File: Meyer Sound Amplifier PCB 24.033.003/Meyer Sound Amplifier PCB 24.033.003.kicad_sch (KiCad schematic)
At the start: 80 parts, among them Q10 KSP92, Q11 KSP92, Q1A IRFP940, Q2A IRFP9240, Q3A TIP29CG, Q4A IRFP914, Q5A IRFP9140, Q6A FEP16BT, Q7A FEP16BT, Q8A TIP50G, Q9 MPSA42, U1 NE5532, U2 LF347N, U3 LM339

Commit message: fix some small errors and missing values
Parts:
- added C18, C23, C24: 1u, symbol Device:C_Small
- added C21, C22: 100n, symbol Device:C_Small
- C1, C5, C6: value ~ -> 470p
- C12: renamed from C12?; value ~ -> 470p
- C13: value 1n -> 1n6
- C14: renamed from C14?; value ~ -> 100n
- C19: renamed from C13??; value ~ -> 100n
- C20: value ~ -> 100n
- C4, C9: value C_Foil -> 22n 250V
- D1, D11, D7: value 10V -> 10V 1N5240B
- D12, D6, D9: value ~ -> 1N4936
- D13: value ~ -> 8.2V? 1N5237B?
- D4: value D_Zener_Dual_CommonCathode_AKA -> 10V 1N5240B
- D5: value ~ -> 10V 1N5240B
- D8: value 10V -> 16V 1N4745
- Q1A: value IRFP940 -> IRFP240
- Q4A: value IRFP914 -> IRFP140
- R23: value 1k/110? -> 1k
- R26: value 3k32? -> 3k32
- VR1: value ~ -> 10k
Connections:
- net GNDA: now also C12.1; no longer R17.1, R18AB.2, R18B.1
- net GNDB: now also R18AB.2, R18B.1
- net at R17.2: now also D11.2 (A), Q5A.1 (G), R16.1; no longer C12.1
- new net: C12.2, R17.1
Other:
- moved on the sheet: C1, C12, C4, D10, D11, D2, D9, Q8A, R1, R16, R17, R2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

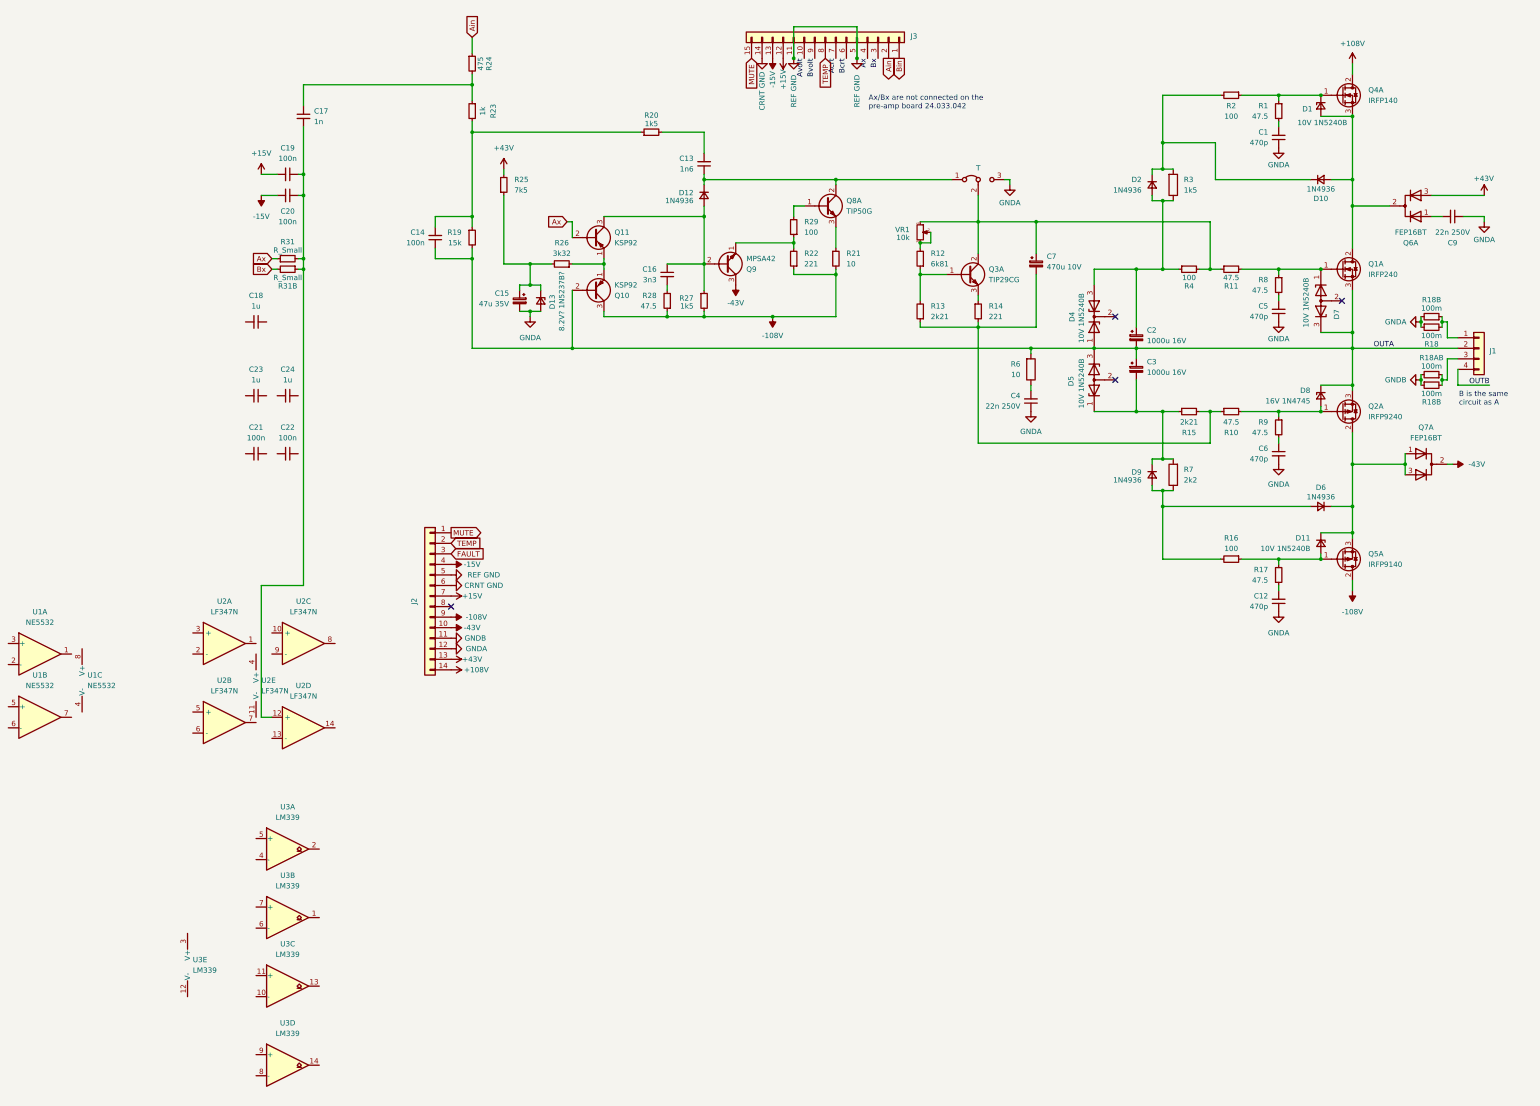
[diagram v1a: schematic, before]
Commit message: some more rev eng and better grouping of parts
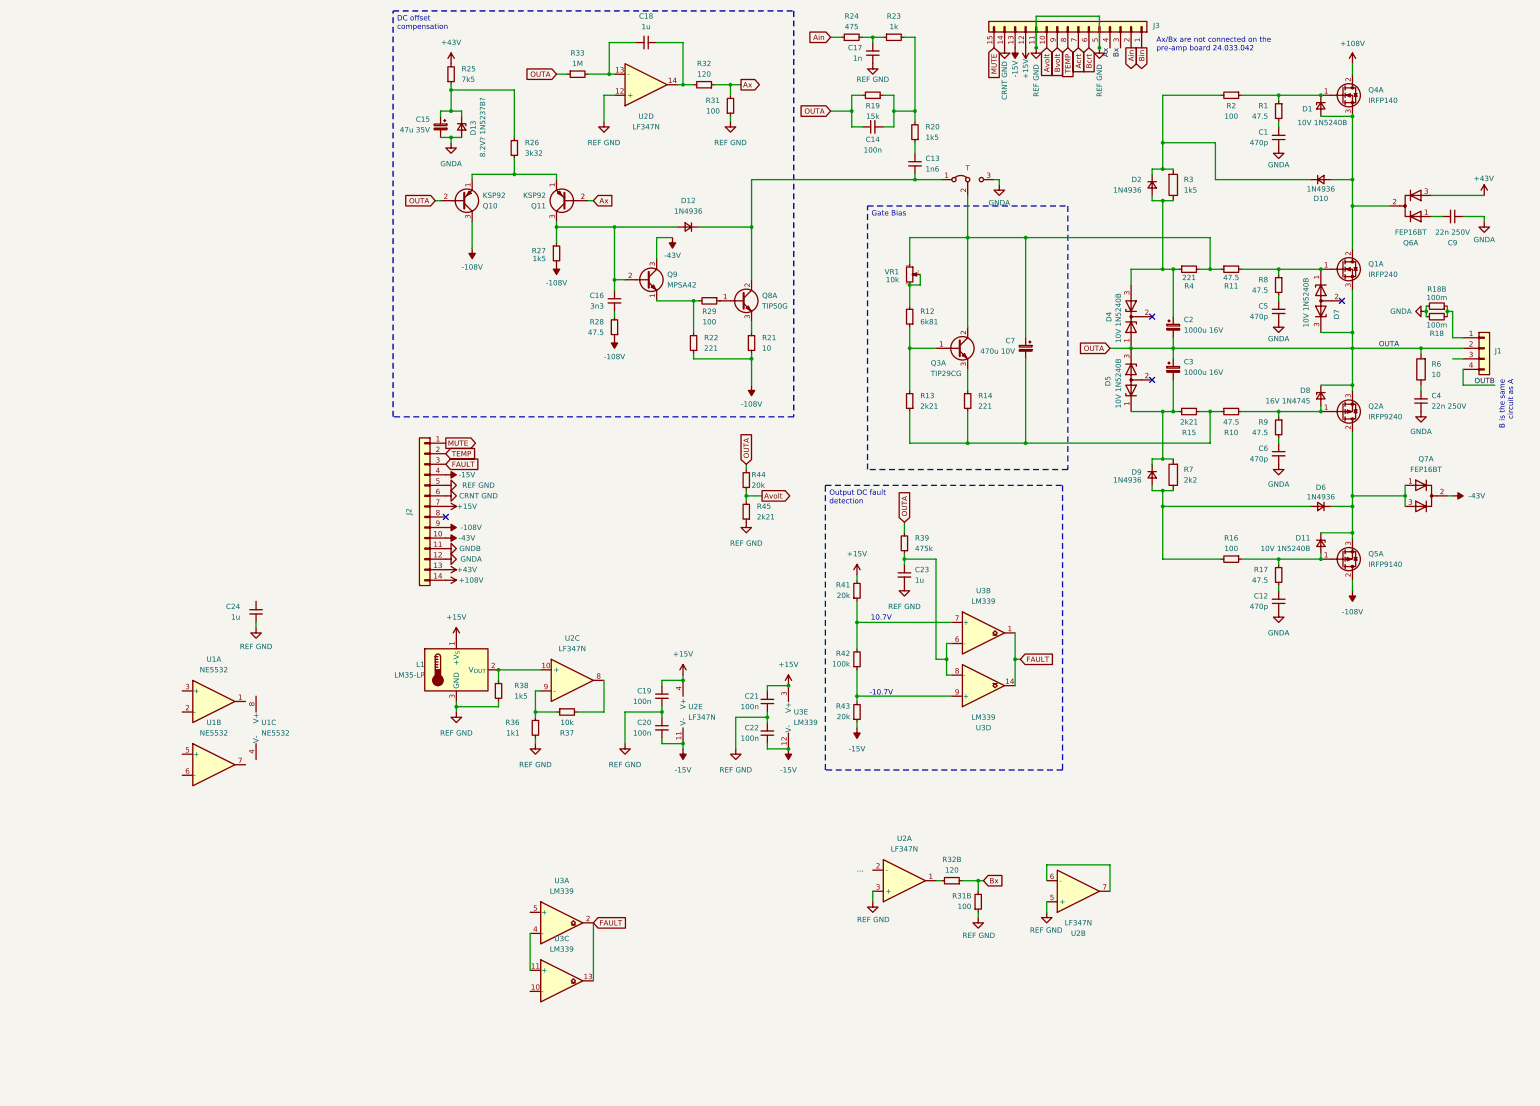
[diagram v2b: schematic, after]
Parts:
- removed R18AB, R18B: 100m, symbol Device:R_Small
- added L1: LM35-LP, Package_TO_SOT_THT:TO-92_Inline, symbol Sensor_Temperature:LM35-LP
- added R32, R32B: 120, symbol Device:R_Small
- added R33: 1M, symbol Device:R_Small
- added R36: 1k1, symbol Device:R_Small
- added R37: 10k, symbol Device:R_Small
- added R38: 1k5, symbol Device:R_Small
- added R39: 475k, symbol Device:R_Small
- added R41, R43, R44: 20k, symbol Device:R_Small
- added R42: 100k, symbol Device:R_Small
- added R45: 2k21, symbol Device:R_Small
- R31, R31B: value R_Small -> 100
- R4: value 100 -> 221
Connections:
- net +15V: now also C19.1, C21.2, U2.4 (V+), U3.3 (V+), L1.1 (+V_{S}), R41.2; no longer C19.2
- net -15V: now also C22.1, U2.11 (V-), U3.12 (V-), R43.1
- net Avolt: now also R44.1, R45.2
- net Ax: now also R31.2, R32.1; no longer R31.1
- net Bx: now also R32B.1
- net FAULT: now also U3.1, U3.13, U3.14, U3.2
- net OUTA: now also R33.1, R39.2, R44.2
- net REF GND: now also C17.1, C19.2, C20.1, C21.1, C22.2, C23.2, C24.2, R31.1, R31B.1, U2.12 (+), U2.3 (+), U2.5 (+), L1.3 (GND), R36.2, R38.2, R45.1
- net at U3.8 (-): now also C23.1, U3.6 (-), R39.1
- net at U3.9 (+): now also R42.1, R43.2
- net at D12.1 (K), Q8A.2 (C), T.1 (A): now also C13.2; no longer C13.1
- net at R20.2: now also C14.2, R19.1, R23.2; no longer C13.2
- net at Q9.1 (E), R22.2: now also R29.2; no longer R29.1
- net at Q8A.1 (B): now also R29.1; no longer R29.2
- net at U3.4 (-): now also U3.11 (+)
- net at C15.1, D13.1 (K), R25.1: now also R26.1; no longer R26.2
- net at C18.1: now also U2.14, R32.2
- net at C18.2: now also U2.13 (-), R33.2
- net at R23.1, R24.2: now also C17.2; no longer C17.1
- net at U3.7 (+): now also R41.1, R42.2
- net at U2.10 (+): now also L1.2 (V_{OUT}), R38.1
- net at U2.8: now also R37.2
- net at U2.9 (-): now also R36.1, R37.1
- net at Q10.1 (E), Q11.1 (E): now also R26.2; no longer R26.1
- net at U2.6 (-): now also U2.7
- net at U2.1: now also R32B.2
- new net: C13.1, R20.1
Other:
- note added: "-10.7V"
- note added: "..."
- note added: "10.7V"
- moved on the sheet: C13, C14, C15, C16, C17, C18, C19, C2, C20, C21, C22, C23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

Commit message: add current feedback and some minor fixes
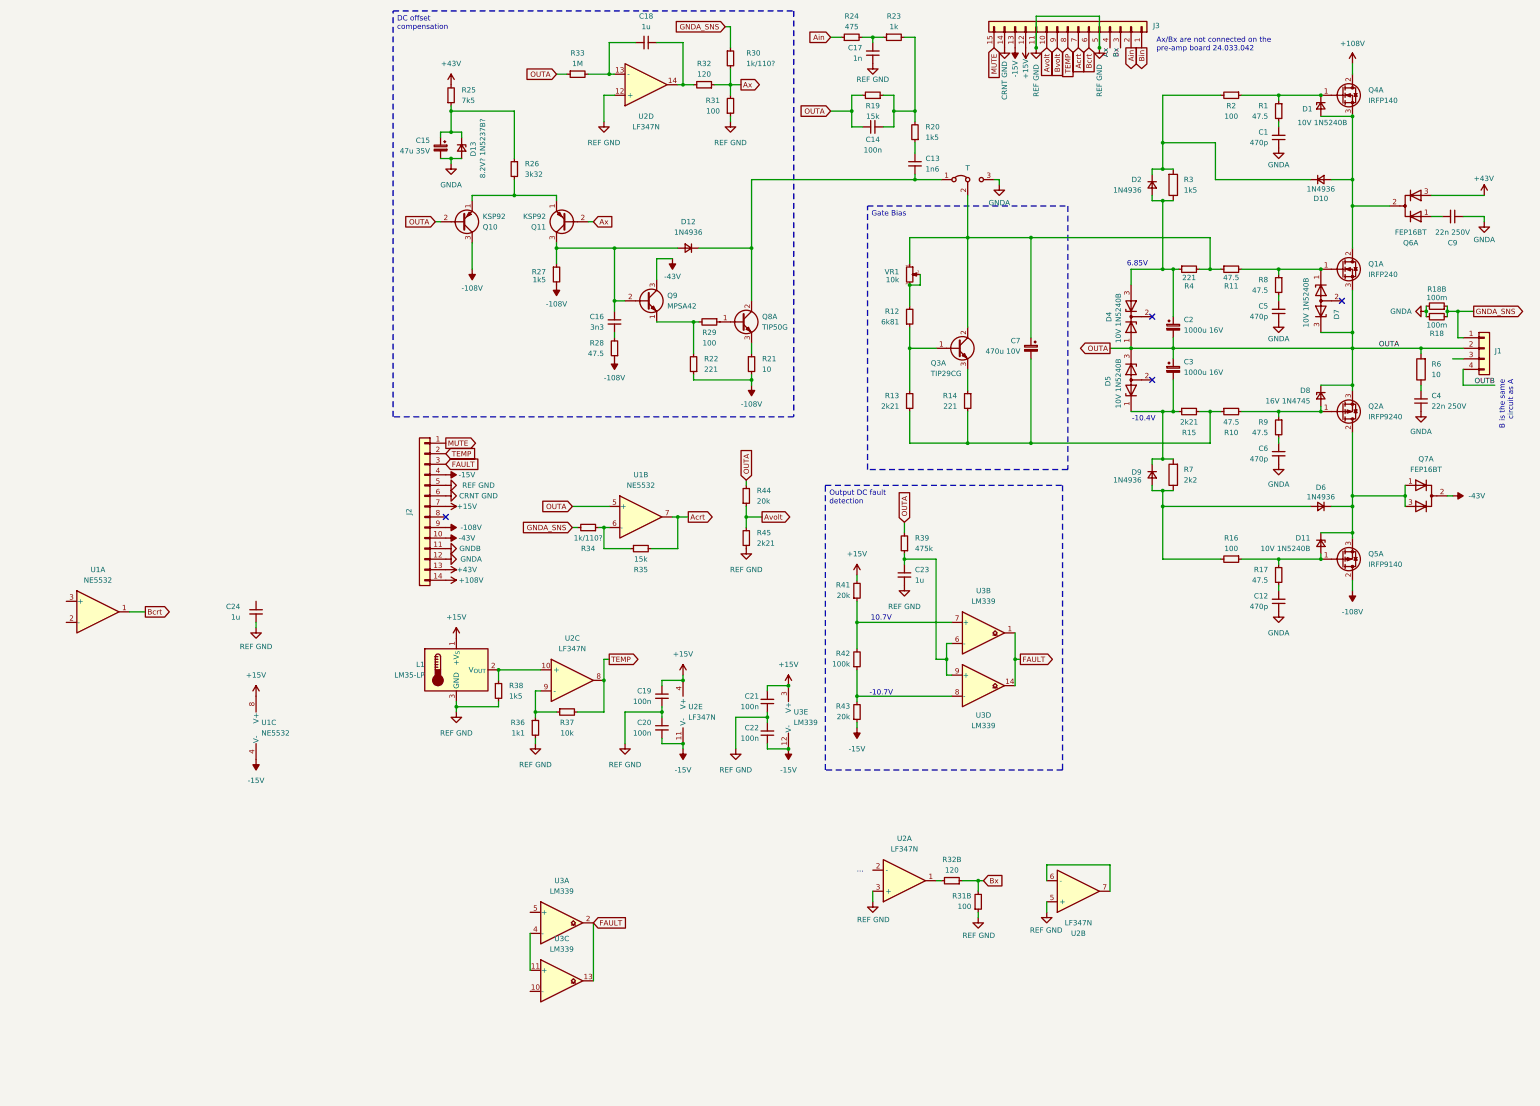
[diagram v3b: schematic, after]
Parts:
- added R30, R34: 1k/110?, symbol Device:R_Small
- added R35: 15k, symbol Device:R_Small
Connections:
- net +15V: now also U1.8 (V+)
- net -15V: now also U1.4 (V-)
- net Acrt: now also U1.7, R35.2
- net Ax: now also R30.2
- net Bcrt: now also U1.1
- net OUTA: now also U1.5 (+)
- net TEMP: now also R37.2, U2.8
- net at C23.1, R39.1, U3.6 (-): now also U3.9 (+); no longer U3.8 (-)
- net at R42.1, R43.2: now also U3.8 (-); no longer U3.9 (+)
- net GNDA_SNS: now reaches J1.1 (Pin_1), R18.2, R18B.1
- net GNDA_SNS: now also R30.1, R34.2
- net at U1.6 (-): now also R34.1, R35.1
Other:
- note added: "-10.4V"
- note added: "6.85V"
- moved on the sheet: C15, C16, C7, D12, D13, Q10, Q11, Q8A, Q9, R12, R13, R21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
